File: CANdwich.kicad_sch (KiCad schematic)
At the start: 48 parts, among them J3 DE9_Receptacle, J4 Conn_01x04_Socket, J5 USB_C_Receptacle_USB2.0, U1 AP2127K-3.3, U2 STM32F072CBT6, U3 SN6505BDBV, U5 AP2204RA-5.0, U6 ISO1050DUB, Y1 16MHz

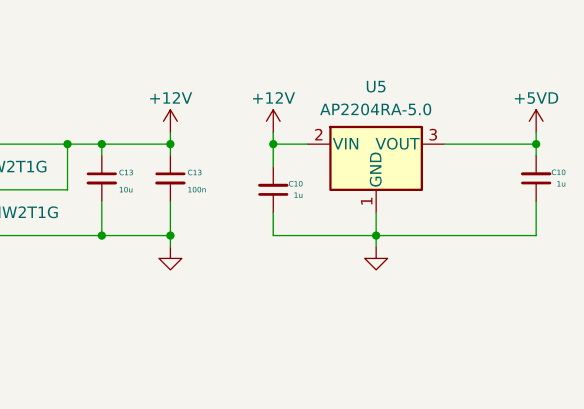
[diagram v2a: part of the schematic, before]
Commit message: resize edge.cuts
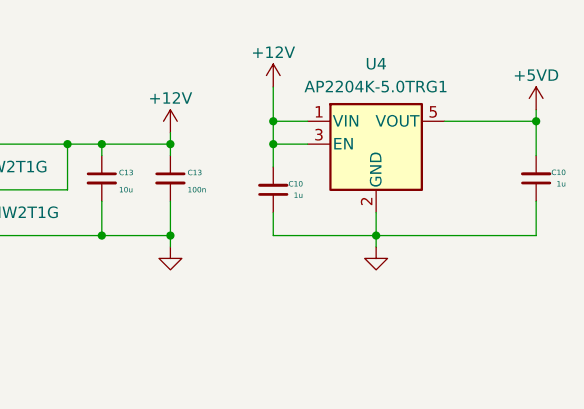
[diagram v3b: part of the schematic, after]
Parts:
- removed U5: AP2204RA-5.0, Package_TO_SOT_SMD:SOT-89-3, symbol Regulator_Linear:AP2204RA-5.0
- added U4: AP2204K-5.0TRG1, Package_TO_SOT_SMD:SOT-23-5, symbol Regulator_Linear:AP2127K-3.3
- TP? (x9): footprint TestPoint:TestPoint_Pad_D1.5mm -> TestPoint:TestPoint_Pad_D1.0mm
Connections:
- net +12V: now also U4.1 (VIN), U4.3 (EN)
- net +5VD: now also U4.5 (VOUT)
- net GNDA: now also U4.2 (GND)
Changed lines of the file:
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@@
   (junction (at 227.33 53.34) (diameter 0) (color 0 0 0 0)
   )
+  (junction (at 238.76 40.64) (diameter 0) (color 0 0 0 0)
+  )
   (junction (at 88.9 62.23) (diameter 0) (color 0 0 0 0)
   )
@@
   (junction (at 250.19 53.34) (diameter 0) (color 0 0 0 0)
   )
-  (junction (at 267.97 43.18) (diameter 0) (color 0 0 0 0)
+  (junction (at 267.97 40.64) (diameter 0) (color 0 0 0 0)
   )
   (junction (at 238.76 43.18) (diameter 0) (color 0 0 0 0)
@@
     (stroke (width 0) (type default))
   )
-  (wire (pts (xy 267.97 41.91) (xy 267.97 43.18))
+  (wire (pts (xy 267.97 39.37) (xy 267.97 40.64))
     (stroke (width 0) (type default))
   )
-  (wire (pts (xy 257.81 43.18) (xy 267.97 43.18))
+  (wire (pts (xy 257.81 40.64) (xy 267.97 40.64))
     (stroke (width 0) (type default))
   )
@@
     (stroke (width 0) (type default))
   )
+  (wire (pts (xy 238.76 40.64) (xy 242.57 40.64))
+    (stroke (width 0) (type default))
+  )
   (wire (pts (xy 238.76 43.18) (xy 238.76 45.72))
     (stroke (width 0) (type default))
@@
     (stroke (width 0) (type default))
   )
-  (wire (pts (xy 267.97 44.45) (xy 267.97 43.18))
+  (wire (pts (xy 267.97 40.64) (xy 267.97 44.45))
     (stroke (width 0) (type default))
   )
@@
     (stroke (width 0) (type default))
   )
+  (wire (pts (xy 238.76 40.64) (xy 238.76 43.18))
+    (stroke (width 0) (type default))
+  )
   (wire (pts (xy 161.29 173.99) (xy 161.29 176.53))
     (stroke (width 0) (type default))
@@
     (stroke (width 0) (type default))
   )
-  (wire (pts (xy 238.76 41.91) (xy 238.76 43.18))
+  (wire (pts (xy 238.76 36.83) (xy 238.76 40.64))
     (stroke (width 0) (type default))
   )
@@
       (effects (font (size 1.27 1.27)) (justify left) hide)
     )
-    (property "Footprint" "TestPoint:TestPoint_Pad_D1.5mm" (at 77.47 62.23 0)
+    (property "Footprint" "TestPoint:TestPoint_Pad_D1.0mm" (at 77.47 62.23 0)
       (effects (font (size 1.27 1.27)) hide)
     )
@@
     )
   )
-  (symbol (lib_id "Regulator_Linear:AP2204RA-5.0") (at 250.19 43.18 0) (unit 1)
-    (in_bom yes) (on_board yes) (dnp no) (fields_autoplaced)
-    (property "Reference" "U5" (at 250.19 36.83 0)
-      (effects (font (size 1.27 1.27)))
-    )
-    (property "Value" "AP2204RA-5.0" (at 250.19 39.37 0)
-      (effects (font (size 1.27 1.27)))
-    )
-    (property "Footprint" "Package_TO_SOT_SMD:SOT-89-3" (at 250.19 37.465 0)
-      (effects (font (size 1.27 1.27)) hide)
-    )
-    (property "Datasheet" "https://www.diodes.com/assets/Datasheets/AP2204.pdf" (at 250.19 43.18 0)
-      (effects (font (size 1.27 1.27)) hide)
-    )
-    (property "LCSC" "C112030" (at 250.19 43.18 0)
-      (effects (font (size 1.27 1.27)) hide)
-    )
-    (property "Mfr" "Diodes" (at 250.19 43.18 0)
-      (effects (font (size 1.27 1.27)) hide)
-    )
-    (property "PN" "ISO1050DUB" (at 250.19 43.18 0)
-      (effects (font (size 1.27 1.27)) hide)
-    )
-    (pin "1")
-    (pin "2")
-    (pin "3")
-    (instances
-      (project "CANdwich"
-        (path "/ba121725-8651-4518-b802-e729710bae45"
-          (reference "U5") (unit 1)
-        )
-      )
-    )
-  )
   (symbol (lib_id "Device:Crystal_GND24_Small") (at 60.96 86.36 180) (unit 1)
     (in_bom yes) (on_board yes) (dnp no)
@@
       (effects (font (size 1.27 1.27)) (justify left) hide)
     )
-    (property "Footprint" "TestPoint:TestPoint_Pad_D1.5mm" (at 167.64 193.04 0)
+    (property "Footprint" "TestPoint:TestPoint_Pad_D1.0mm" (at 167.64 193.04 0)
       (effects (font (size 1.27 1.27)) hide)
     )
@@
       (effects (font (size 1.27 1.27)) (justify left) hide)
     )
-    (property "Footprint" "TestPoint:TestPoint_Pad_D1.5mm" (at 172.72 195.58 0)
+    (property "Footprint" "TestPoint:TestPoint_Pad_D1.0mm" (at 172.72 195.58 0)
       (effects (font (size 1.27 1.27)) hide)
     )
@@
     )
   )
-  (symbol (lib_id "power:+12V") (at 238.76 41.91 0) (unit 1)
+  (symbol (lib_id "power:+12V") (at 238.76 36.83 0) (unit 1)
     (in_bom yes) (on_board yes) (dnp no) (fields_autoplaced)
-    (property "Reference" "#PWR046" (at 238.76 45.72 0)
+    (property "Reference" "#PWR046" (at 238.76 40.64 0)
       (effects (font (size 1.27 1.27)) hide)
     )
-    (property "Value" "+12V" (at 238.76 38.1 0)
+    (property "Value" "+12V" (at 238.76 33.02 0)
       (effects (font (size 1.27 1.27)))
     )
-    (property "Footprint" "" (at 238.76 41.91 0)
+    (property "Footprint" "" (at 238.76 36.83 0)
       (effects (font (size 1.27 1.27)) hide)
     )
-    (property "Datasheet" "" (at 238.76 41.91 0)
+    (property "Datasheet" "" (at 238.76 36.83 0)
       (effects (font (size 1.27 1.27)) hide)
     )
@@
       (effects (font (size 1.27 1.27)) (justify left) hide)
     )
-    (property "Footprint" "TestPoint:TestPoint_Pad_D1.5mm" (at 119.38 109.22 0)
+    (property "Footprint" "TestPoint:TestPoint_Pad_D1.0mm" (at 119.38 109.22 0)
       (effects (font (size 1.27 1.27)) hide)
     )
@@
       (effects (font (size 1.27 1.27)) (justify left) hide)
     )
-    (property "Footprint" "TestPoint:TestPoint_Pad_D1.5mm" (at 119.38 106.68 0)
+    (property "Footprint" "TestPoint:TestPoint_Pad_D1.0mm" (at 119.38 106.68 0)
       (effects (font (size 1.27 1.27)) hide)
     )
@@
       (effects (font (size 1.27 1.27)) (justify left) hide)
     )
-    (property "Footprint" "TestPoint:TestPoint_Pad_D1.5mm" (at 166.37 186.69 0)
+    (property "Footprint" "TestPoint:TestPoint_Pad_D1.0mm" (at 166.37 186.69 0)
       (effects (font (size 1.27 1.27)) hide)
     )
@@
     )
   )
-  (symbol (lib_id "power:+5VD") (at 267.97 41.91 0) (unit 1)
+  (symbol (lib_id "power:+5VD") (at 267.97 39.37 0) (unit 1)
     (in_bom yes) (on_board yes) (dnp no) (fields_autoplaced)
-    (property "Reference" "#PWR047" (at 267.97 45.72 0)
+    (property "Reference" "#PWR047" (at 267.97 43.18 0)
       (effects (font (size 1.27 1.27)) hide)
     )
-    (property "Value" "+5VD" (at 267.97 38.1 0)
+    (property "Value" "+5VD" (at 267.97 35.56 0)
       (effects (font (size 1.27 1.27)))
     )
-    (property "Footprint" "" (at 267.97 41.91 0)
+    (property "Footprint" "" (at 267.97 39.37 0)
       (effects (font (size 1.27 1.27)) hide)
     )
-    (property "Datasheet" "" (at 267.97 41.91 0)
+    (property "Datasheet" "" (at 267.97 39.37 0)
       (effects (font (size 1.27 1.27)) hide)
     )
@@
       (effects (font (size 1.27 1.27)) (justify left) hide)
     )
-    (property "Footprint" "TestPoint:TestPoint_Pad_D1.5mm" (at 134.62 196.85 0)
+    (property "Footprint" "TestPoint:TestPoint_Pad_D1.0mm" (at 134.62 196.85 0)
       (effects (font (size 1.27 1.27)) hide)
     )
@@
       (effects (font (size 1.27 1.27)) (justify left) hide)
     )
-    (property "Footprint" "TestPoint:TestPoint_Pad_D1.5mm" (at 149.86 194.31 0)
+    (property "Footprint" "TestPoint:TestPoint_Pad_D1.0mm" (at 149.86 194.31 0)
       (effects (font (size 1.27 1.27)) hide)
     )
@@
       (effects (font (size 1.27 1.27)) (justify left) hide)
     )
-    (property "Footprint" "TestPoint:TestPoint_Pad_D1.5mm" (at 165.1 181.61 0)
+    (property "Footprint" "TestPoint:TestPoint_Pad_D1.0mm" (at 165.1 181.61 0)
       (effects (font (size 1.27 1.27)) hide)
     )
@@
         )
       )
+    )
+  )
+  (symbol (lib_id "Regulator_Linear:AP2127K-3.3") (at 250.19 43.18 0) (unit 1)
+    (in_bom yes) (on_board yes) (dnp no) (fields_autoplaced)
+    (property "Reference" "U4" (at 250.19 34.29 0)
+      (effects (font (size 1.27 1.27)))
+    )
+    (property "Value" "AP2204K-5.0TRG1" (at 250.19 36.83 0)
+      (effects (font (size 1.27 1.27)))
+    )
+    (property "Footprint" "Package_TO_SOT_SMD:SOT-23-5" (at 250.19 34.925 0)
+      (effects (font (size 1.27 1.27)) hide)
+    )
+    (property "Datasheet" "https://www.diodes.com/assets/Datasheets/AP2204.pdf" (at 250.19 40.64 0)
+      (effects (font (size 1.27 1.27)) hide)
+    )
+    (property "LCSC" "C112031" (at 250.19 43.18 0)
+      (effects (font (size 1.27 1.27)) hide)
+    )
+    (property "Mfr" "Diodes" (at 250.19 43.18 0)
+      (effects (font (size 1.27 1.27)) hide)
+    )
+    (property "PN" "AP2204K-5.0TRG1" (at 250.19 43.18 0)
+      (effects (font (size 1.27 1.27)) hide)
+    )
+    (pin "1")
+    (pin "2")
+    (pin "3")
+    (pin "4")
+    (pin "5")
+    (instances
+      (project "CANdwich"
+        (path "/ba121725-8651-4518-b802-e729710bae45"
+          (reference "U4") (unit 1)
+        )
+      )

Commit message: V1.0 Generate external enclosure
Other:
- title: (none) -> CANdwich
- moved on the sheet: C10, C11, C12, C13, C7, C8, C9, D2, D3, D4, D5, J3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

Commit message: Change USB edge connection interface
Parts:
- J3: now fitted
- J4: footprint 0_terry:USB_snowflake -> 0_terry:USB_EdgeMount; now fitted; now left out of the parts list
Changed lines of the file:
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@@
   )
   (symbol (lib_id "Connector:DE9_Receptacle") (at 264.16 110.49 0) (unit 1)
-    (in_bom no) (on_board yes) (dnp yes) (fields_autoplaced)
+    (in_bom no) (on_board yes) (dnp no) (fields_autoplaced)
     (property "Reference" "J3" (at 269.24 109.22 0)
       (effects (font (size 1.27 1.27)) (justify left))
@@
   )
   (symbol (lib_id "Connector:Conn_01x04_Socket") (at 24.13 153.67 0) (mirror y) (unit 1)
-    (in_bom yes) (on_board yes) (dnp yes)
+    (in_bom no) (on_board yes) (dnp no)
     (property "Reference" "J4" (at 24.13 163.83 0)
       (effects (font (size 1.27 1.27)))
@@
       (effects (font (size 1.27 1.27)))
     )
-    (property "Footprint" "0_terry:USB_snowflake" (at 24.13 153.67 0)
+    (property "Footprint" "0_terry:USB_EdgeMount" (at 24.13 153.67 0)
       (effects (font (size 1.27 1.27)) hide)
     )
@@
       (effects (font (size 1.27 1.27)) hide)
     )
-    (property "Datasheet" "https://www.diodes.com/assets/Datasheets/AP2204.pdf" (at 241.3 53.34 0)
-      (effects (font (size 1.27 1.27)) hide)
-    )
+    (property "Datasheet" "https://www.mouser.tw/datasheet/2/115/DIOD_S_A0009553075_1-2512842.pdf" (at 241.3 53.34 0)
+      (effects (font (size 1.27 1.27)) hide)
+    )

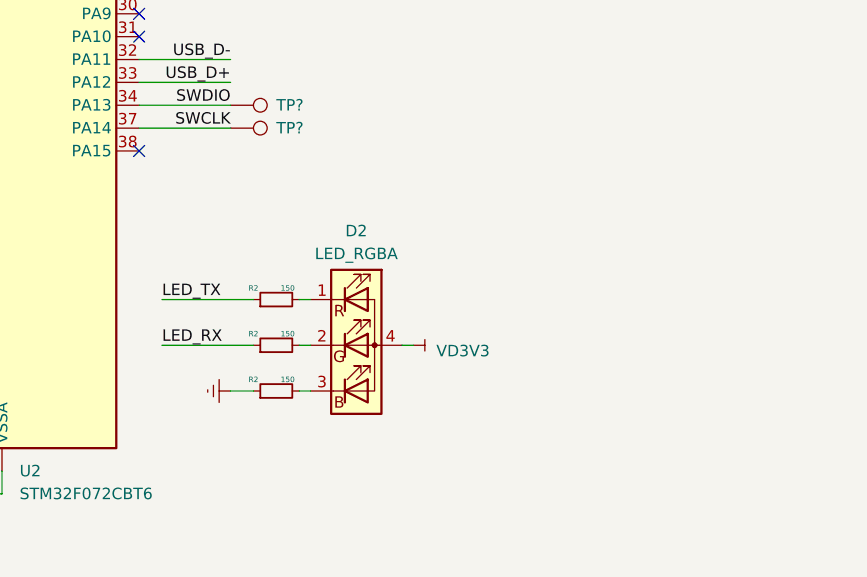
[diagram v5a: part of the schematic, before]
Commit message: Change indication LED
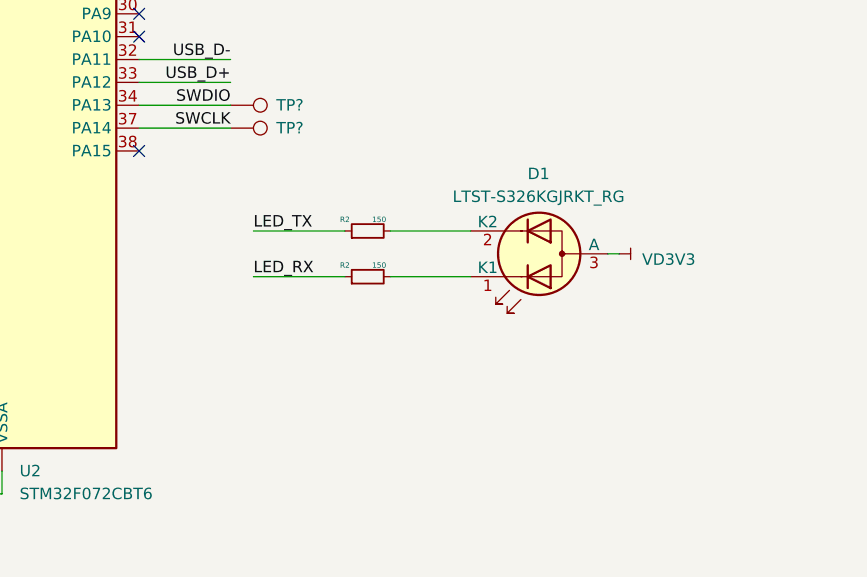
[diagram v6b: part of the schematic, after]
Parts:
- removed D2: LED_RGBA, LED_SMD:LED_LiteOn_LTST-C19HE1WT, symbol Device:LED_RGBA
- removed R2: 150, Resistor_SMD:R_0603_1608Metric, symbol Device:R_Small
- added D1: LTST-S326KGJRKT_RG, 0_terry:LED_LiteOn_LTST-S326, symbol Device:LED_Dual_KKA
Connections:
- net VD3V3: now also D1.3 (A)
- net at R2.2: now also D1.2 (K2)
- net at R2.2: now also D1.1 (K1)
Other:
- moved on the sheet: R2
